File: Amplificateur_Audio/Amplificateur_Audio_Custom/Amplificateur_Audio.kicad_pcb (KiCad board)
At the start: 4 copper layers, 165.7 x 90.1 mm, 855 parts, among them J1101 SURROUND-LEFT, J1102 UPMIX-LEFT, J1103 FR-TWEETER, J1104 FL-TWEETER, J1105 CENTER-TWEETER, J1106 SURROUND-RIGHT, J1107 UPMIX-RIGHT, J1108 FR-WOOFER, J1109 FL-WOOFER, J1110 CENTER-WOOFER, J1111 Analog OUTPUT Connector, J201 JTAG, J202 Conn_01x02, J203 Conn_02x08_Odd_Even, J301 Conn_02x10_Odd_Even, J401 SL+, J402 SL-, J403 SR+, J404 SR-, J405 Analog input Connector, J501 UP LEFT+, J502 UP LEFT-, J503 UP RIGHT+, J504 UP RIGHT-, J601 Front Right Tweeter+, J602 Front Right Tweeter-, J603 Front Right Woofer+, J604 Front Right Woofer-, J701 Front Left Tweeter+, J702 Front Left Tweeter-, J703 Front Left Woofer+, J704 Front Left Woofer-, J801 Center Tweeter+, J802 Center Tweeter-, J803 Center Woofer+, J804 Center Woofer-, J901 I2S-OUT, J902 SUBOUT, Q201 NPN, Q202 NPN, Q203 NPN, Q204 NPN, Q205 NPN, Q206 NPN, Q301 NMOS, Q302 NMOS, SW201 MUTE, SW202 VOL+, SW203 VOL-, SW204 MODE1, SW205 MODE2, SW206 MODE3, SW207 MODE4, SW208 LOAD, SW209 RESET, U1101 NE5532AD, U1102 NE5532AD, U1103 NE5532AD, U1104 NE5532AD, U1105 NE5532AD, U1106 NE5532AD, U1107 NE5532AD, U1108 NE5532AD, U1109 NE5532AD, U1110 NE5532AD, U201 MSP430F5234IRGZ, U202 TCA6408ARSVR, U203 24LC512, U204 TCA9548ARGER, U301 74LVC1G125, U302 74LVC1G125, U303 74LVC1G125, U304 74LVC1G125, U305 74LVC1G125, U306 74LVC1G125, U307 74LVC1G125, U308 74LVC1G125, U309 74LVC1G125, U310 74LVC1G125, U401 PCM5252RHBR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

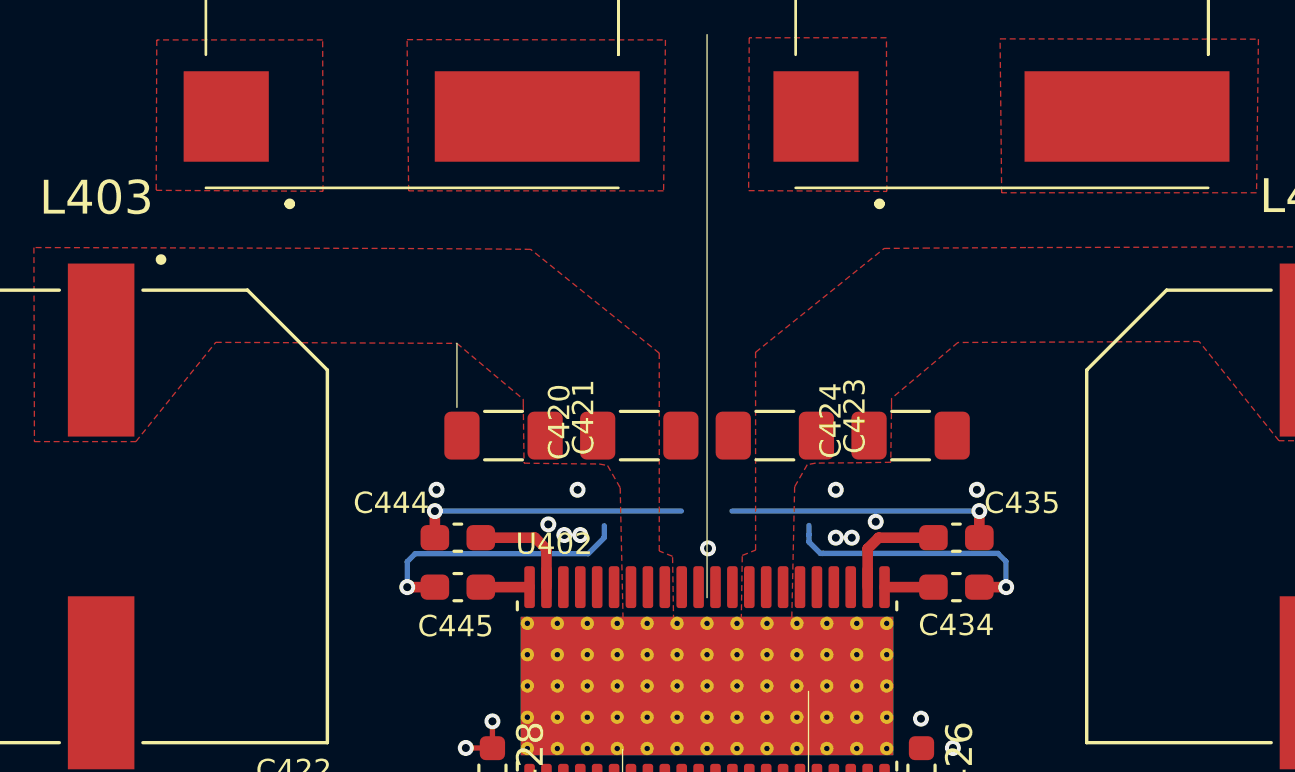
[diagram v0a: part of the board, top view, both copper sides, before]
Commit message: Suite amélioration du routage, PVDD local en top, et plan global couche 3. Passage des sorties audios OUTx en bottom
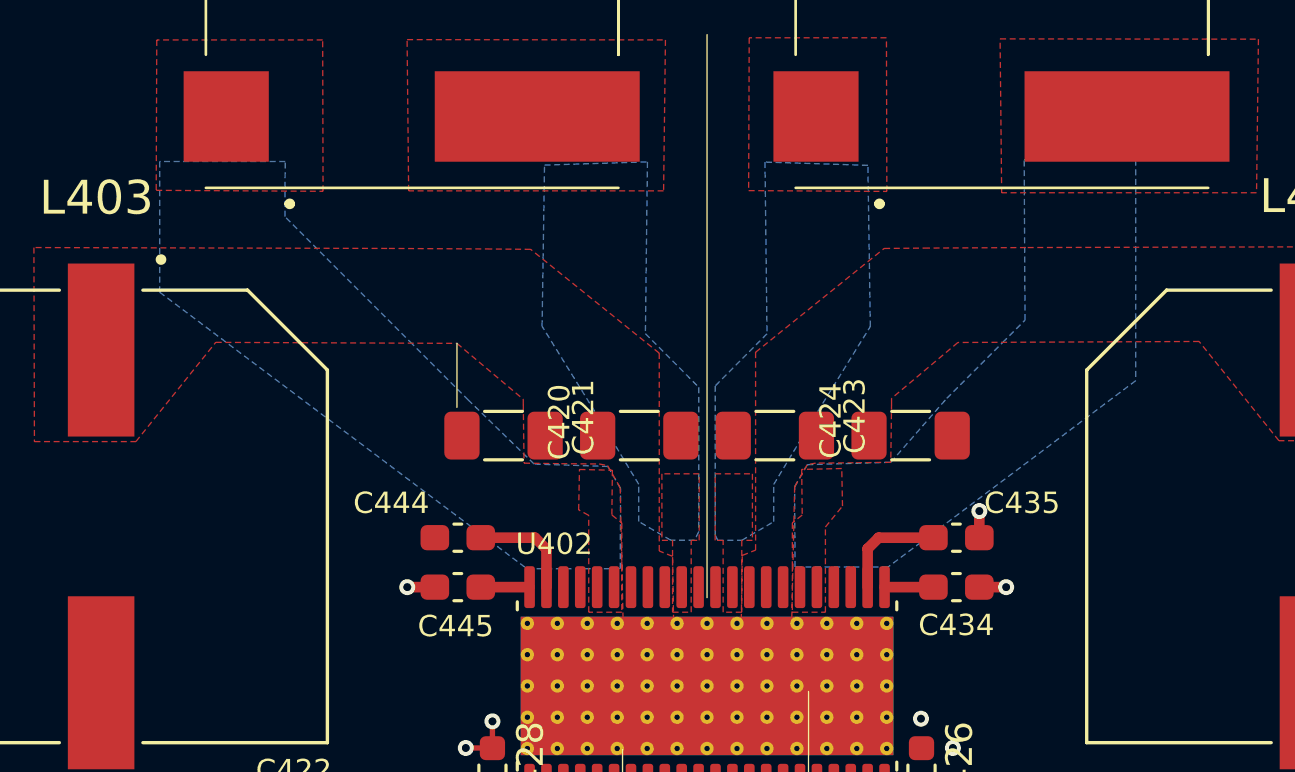
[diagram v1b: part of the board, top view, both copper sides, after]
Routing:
- net /Surrond_Channel/OUT1C: track 10.3 -> 0.00 mm, vias 1 -> 0
- net /Surrond_Channel/OUT1B: track 10.3 -> 1.00 mm
- net /Surrond_Channel/OUT1A: track 10.3 -> 1.01 mm
- net /Surrond_Channel/OUT1D: track 10.2 -> 1.04 mm
- net GND: vias 83 -> 72
- added copper zone on B.Cu, net /Surrond_Channel/OUT1A
- added copper zone on B.Cu, net /Surrond_Channel/OUT1B
- added copper zone on B.Cu, net /Surrond_Channel/OUT1C
- added copper zone on B.Cu, net /Surrond_Channel/OUT1D

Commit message: Suite routage amélioré
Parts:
- moved C422 1.70 mm to (102.1, 75.0)
- moved C425 1.70 mm to (144.3, 75.0)
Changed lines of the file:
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@@
 	(footprint "NewLibrary:CAP_EEVFK1H102M"
 		(layer "F.Cu")
-		(at 100.4325 75.0005 -90)
+		(at 102.1325 75.0005 -90)
 		(property "Reference" "C422"
-			(at 9.5395 -7.24 180)
+			(at 9.5395 -7.24 0)
 			(layer "F.SilkS")
 			(effects
@@
 	(footprint "NewLibrary:CAP_EEVFK1H102M"
 		(layer "F.Cu")
-		(at 145.9585 75.0005 -90)
+		(at 144.2585 75.0005 -90)
 		(property "Reference" "C425"
-			(at 9.4995 -7.074 180)
+			(at 9.4995 -7.074 0)
 			(layer "F.SilkS")
 			(effects
@@
 		(polygon
 			(pts
-				(xy 122.9 73.4) (xy 121.5 73.4) (xy 121.5 75.9) (xy 121.9 75.9) (xy 121.9 78.6) (xy 122.6 78.6)
-				(xy 122.6 75.9) (xy 122.9 75.9)
+				(xy 122.9 73.4) (xy 121.6 73.4) (xy 121.6 76.2) (xy 121.9 76.2) (xy 121.9 78.6) (xy 122.6 78.6)
+				(xy 122.6 76.2) (xy 122.9 76.2)
 			)
 		)
@@
 		(polygon
 			(pts
-				(xy 123.5 73.4) (xy 124.9 73.4) (xy 124.9 75.9) (xy 124.5 75.9) (xy 124.5 78.6) (xy 123.8 78.6)
-				(xy 123.8 75.9) (xy 123.5 75.9)
+				(xy 123.5 73.4) (xy 124.9 73.4) (xy 124.9 76.2) (xy 124.5 76.2) (xy 124.5 78.6) (xy 123.8 78.6)
+				(xy 123.8 76.2) (xy 123.5 76.2)
 			)
 		)
@@
 		(polygon
 			(pts
-				(xy 97.907629 64.9) (xy 97.926238 72.19) (xy 101.73845 72.19) (xy 104.738461 68.461539) (xy 113.8 68.5)
+				(xy 99.31376 64.903532) (xy 99.332361 72.19) (xy 103.957878 72.19) (xy 106.950335 68.470928) (xy 113.8 68.5)
 				(xy 116.291875 70.6) (xy 116.291875 70.796114) (xy 116.320589 72.999981) (xy 117.720241 73.020513)
 				(xy 119.142947 73.030769) (xy 119.458974 73.090695) (xy 119.9325 73.92) (xy 120.041216 78.910044)
@@
 			(pts
 				(xy 117.090008 61.8027) (xy 120.955842 61.680896) (xy 120.879503 68.132197) (xy 122.885529 70.149866)
-				(xy 122.885529 75.577084) (xy 122.728046 75.892049) (xy 121.828046 75.892049) (xy 120.628046 75.192049)
+				(xy 122.885529 75.577084) (xy 122.578045 76.192049) (xy 121.899465 76.192049) (xy 120.628046 75.450388)
 				(xy 120.628046 73.792049) (xy 118.978046 71.058441) (xy 116.998245 67.859092)
 			)
@@
 			(pts
 				(xy 129.238038 61.810651) (xy 125.372204 61.688847) (xy 125.448543 68.140148) (xy 123.5 70.1) (xy 123.5 75.7)
-				(xy 123.6 75.9) (xy 124.5 75.9) (xy 125.7 75.2) (xy 125.7 73.8) (xy 127.35 71.066392) (xy 129.329801 67.867043)
+				(xy 123.75 76.2) (xy 124.500004 76.2) (xy 125.7 75.500002) (xy 125.7 73.8) (xy 127.35 71.066392)
+				(xy 129.329801 67.867043)
 			)
 		)
